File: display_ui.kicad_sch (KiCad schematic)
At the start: 68 parts, among them SW401 K2-1102SP-C4SC-04, SW402 K2-1102SP-C4SC-04, SW403 K2-1102SP-C4SC-04, SW404 K2-1102SP-C4SC-04, T401 AO3400A, T402 AO3400A, T403 AO3400A, T404 AO3400A, T405 AO3400A, X401 ER-TFT035-6

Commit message: changed pin types and fixed 3D-positions
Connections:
- removed net +3.3V: BUZZER401.1 (+), C409.2, C410.2, C411.2, D409.3 (A), D411.1 (K), R401.2, R404.3, R408.2, R411.3, R415.3, R416.2, R420.2, R428.1, R430.1, R433.1, R435.2, X401.13 (DOTCLK), X401.35 (RD), X401.40 (VDDI), X401.41 (VDDI), X401.42 (VCI)
- removed net GND: C401.1, C402.1, C403.1, C404.1, C405.1, C406.1, C407.1, C408.1, C409.1, C410.1, C411.1, D401.2 (C), D402.2 (C), D403.2 (C), D404.2 (C), D405.2 (C), D406.2 (C), D407.2 (C), D408.2 (C), D410.3 (VSS), R402.1, R404.1, R409.1, R411.1, R415.1, R417.1, R421.1, R429.2, R431.2, R434.2, T401.2 (S), T402.2 (S), T403.2 (S), T404.2 (S), T405.2 (S), X401.11 (VSYNC), X401.12 (HSYNC), X401.14 (DE), X401.15 (DB17), X401.16 (DB16), X401.17 (DB15), X401.18 (DB14), X401.19 (DB13), X401.20 (DB12), X401.21 (DB11), X401.22 (DB10), X401.23 (DB9), X401.24 (DB8), X401.25 (DB7), X401.26 (DB6), X401.27 (DB5), X401.28 (DB4), X401.29 (DB3), X401.30 (DB2), X401.31 (DB1), X401.32 (DB0), X401.43 (GND), X401.48 (GND), X401.49 (GND), X401.50 (GND)
- new net: C409.1, C410.1, C411.1
- new net: C409.2, C410.2, C411.2
- new net: R428.1, R430.1, R433.1
- new net: BUZZER401.1 (+), D411.1 (K)
- new net: X401.11 (VSYNC), X401.12 (HSYNC)
- new net: X401.14 (DE), X401.15 (DB17), X401.16 (DB16), X401.17 (DB15), X401.18 (DB14), X401.19 (DB13), X401.20 (DB12), X401.21 (DB11), X401.22 (DB10), X401.23 (DB9), X401.24 (DB8), X401.25 (DB7), X401.26 (DB6), X401.27 (DB5), X401.28 (DB4), X401.29 (DB3), X401.30 (DB2), X401.31 (DB1), X401.32 (DB0)
- new net: X401.40 (VDDI), X401.41 (VDDI), X401.42 (VCI)
- new net: X401.48 (GND), X401.49 (GND), X401.50 (GND)
- new net: R429.2, R431.2, R434.2

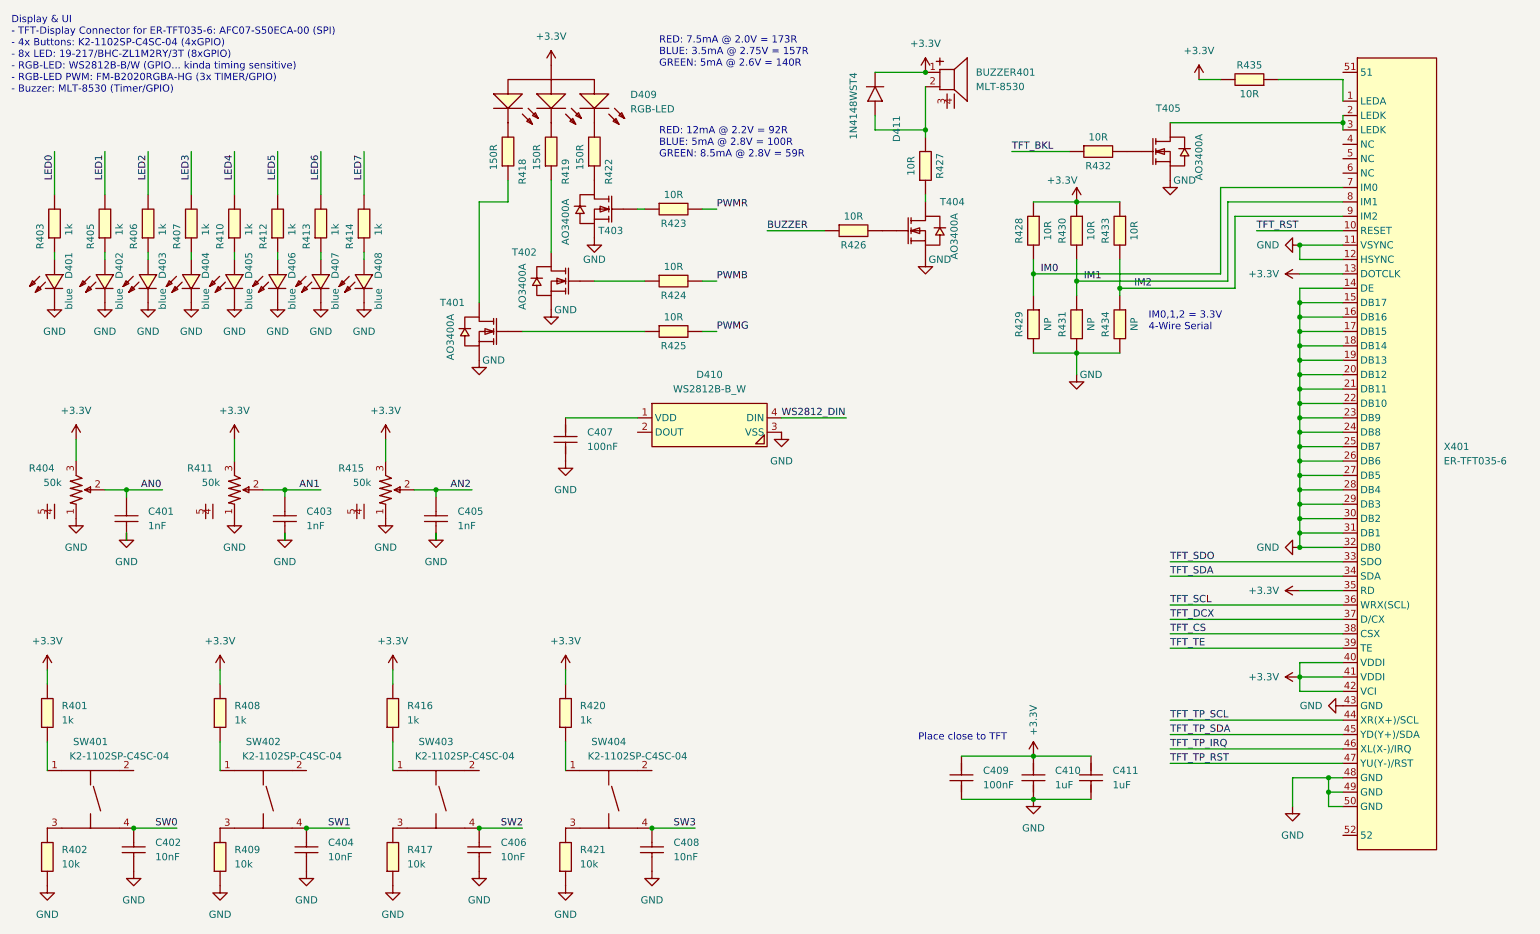
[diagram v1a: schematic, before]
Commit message: change all local labels to global labels.
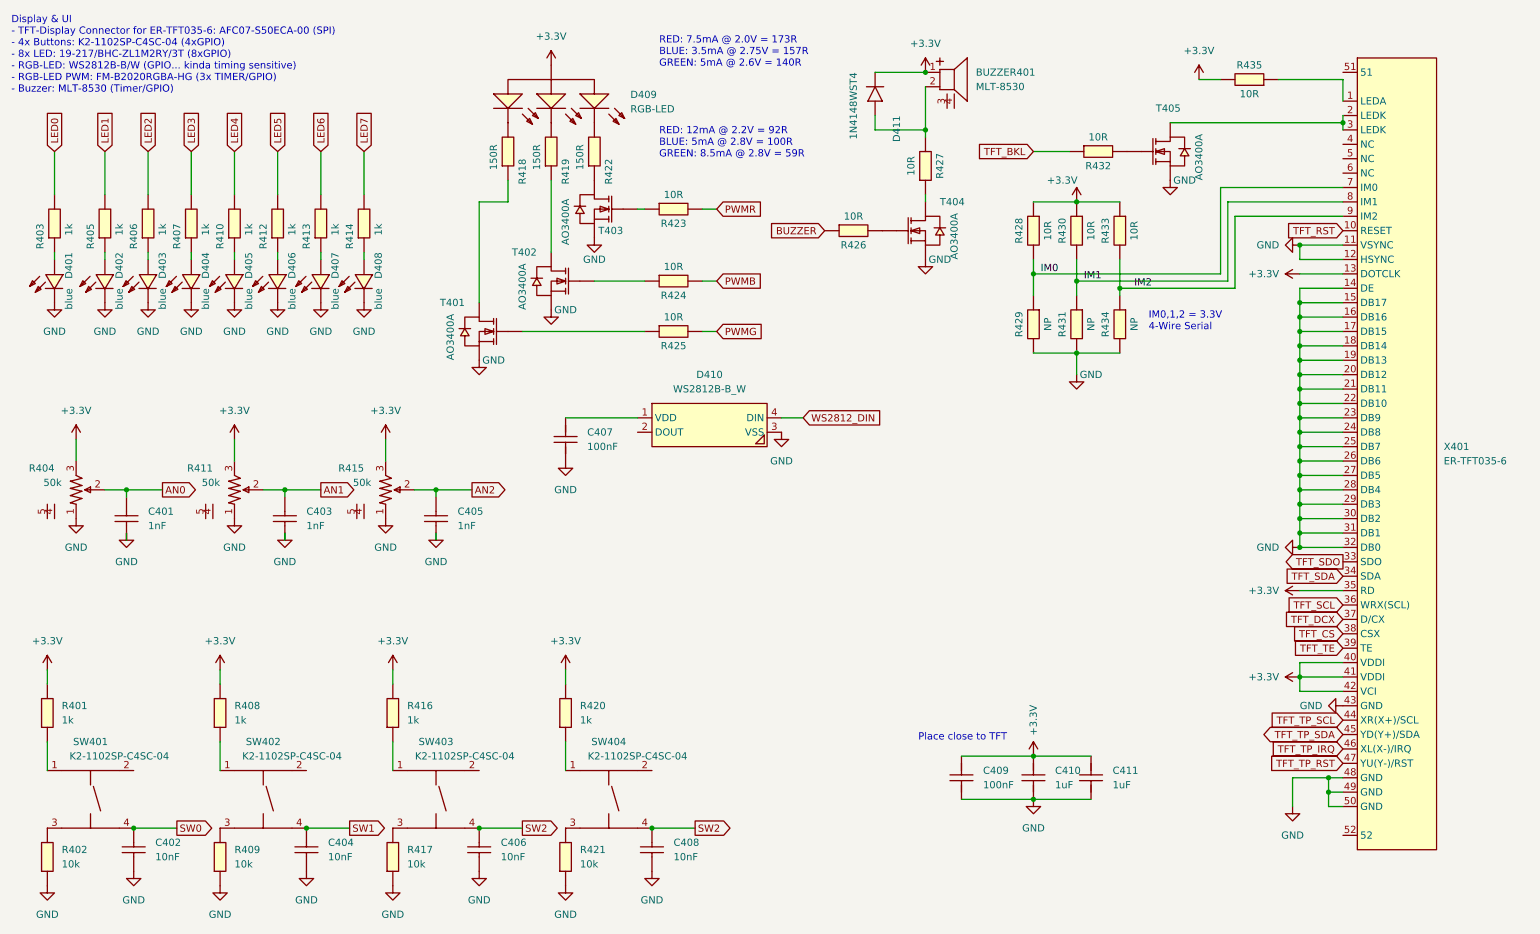
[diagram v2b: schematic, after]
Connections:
- net SW3 is gone; now on net SW2: C408.2, SW404.4

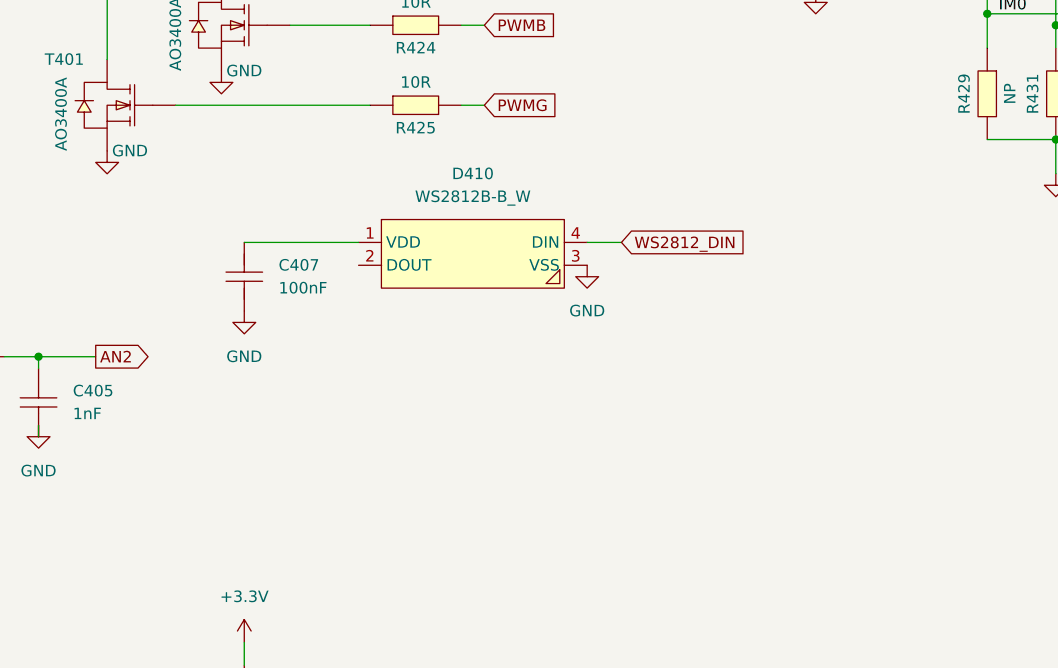
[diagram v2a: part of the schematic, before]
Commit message: add WS2812 Output Connector and add Level shifter to WS2812 input for 3.3V->5V conversion
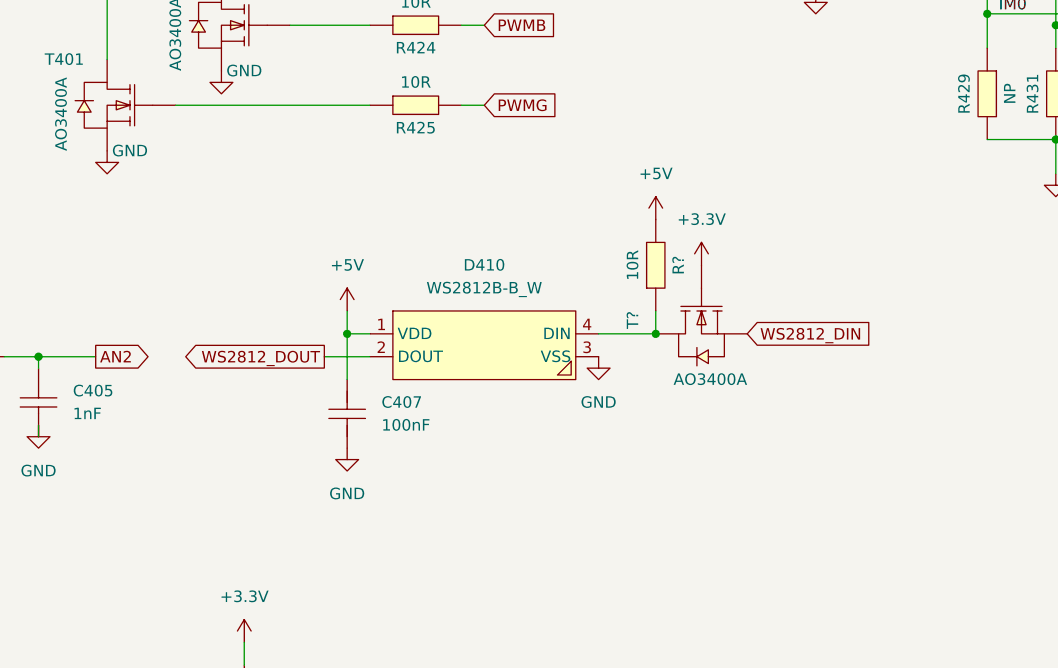
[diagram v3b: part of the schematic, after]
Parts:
- added R?: 10R, R0402, symbol eduboardv2:0402WGF100JTCE
- added T?: AO3400A, SOT-23-3_L2.9-W1.6-P1.90-LS2.8-BR, symbol eduboardv2:AO3400A
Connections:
- net WS2812_DIN: now also T?.2 (S); no longer D410.4 (DIN)
- net WS2812_DOUT: now reaches D410.2 (DOUT)
- new net: D410.4 (DIN), R?.1, T?.3 (D)
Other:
- moved on the sheet: C407, D410

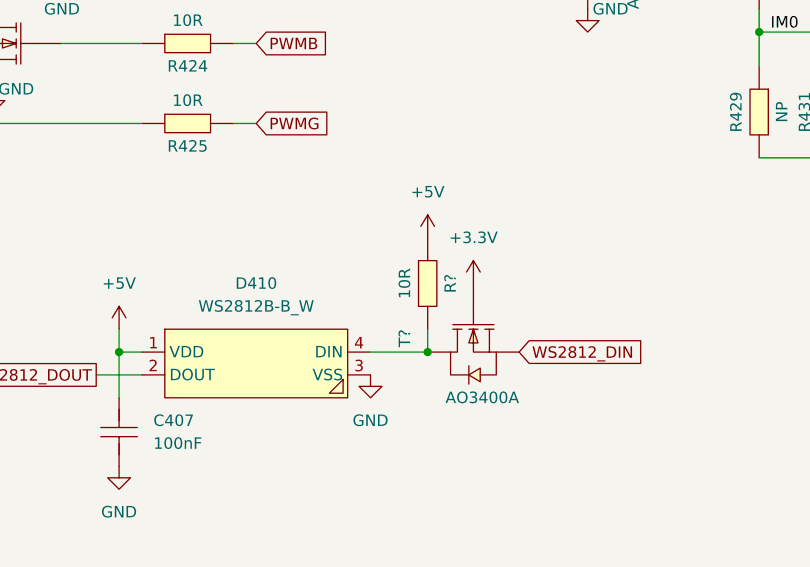
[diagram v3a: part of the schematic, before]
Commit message: fix Resistor Value for WS2812 level shifter
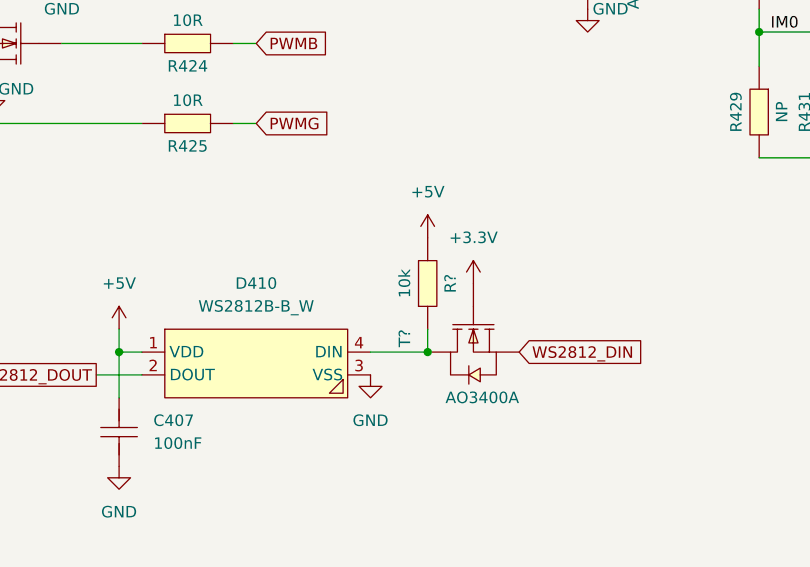
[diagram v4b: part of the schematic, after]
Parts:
- R?: value 10R -> 10k
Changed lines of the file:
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@@
     (in_bom yes) (on_board yes)
     (property "Reference" "R?" (id 0) (at 160.02 87.63 0))
-    (property "Value" "10R" (id 1) (at 154.94 87.63 0))
+    (property "Value" "10k" (id 1) (at 154.94 87.63 0))
     (property "Footprint" "R0402" (id 2) (at 165.1 87.63 0)
       (effects (font (size 1.27 1.27)) hide)

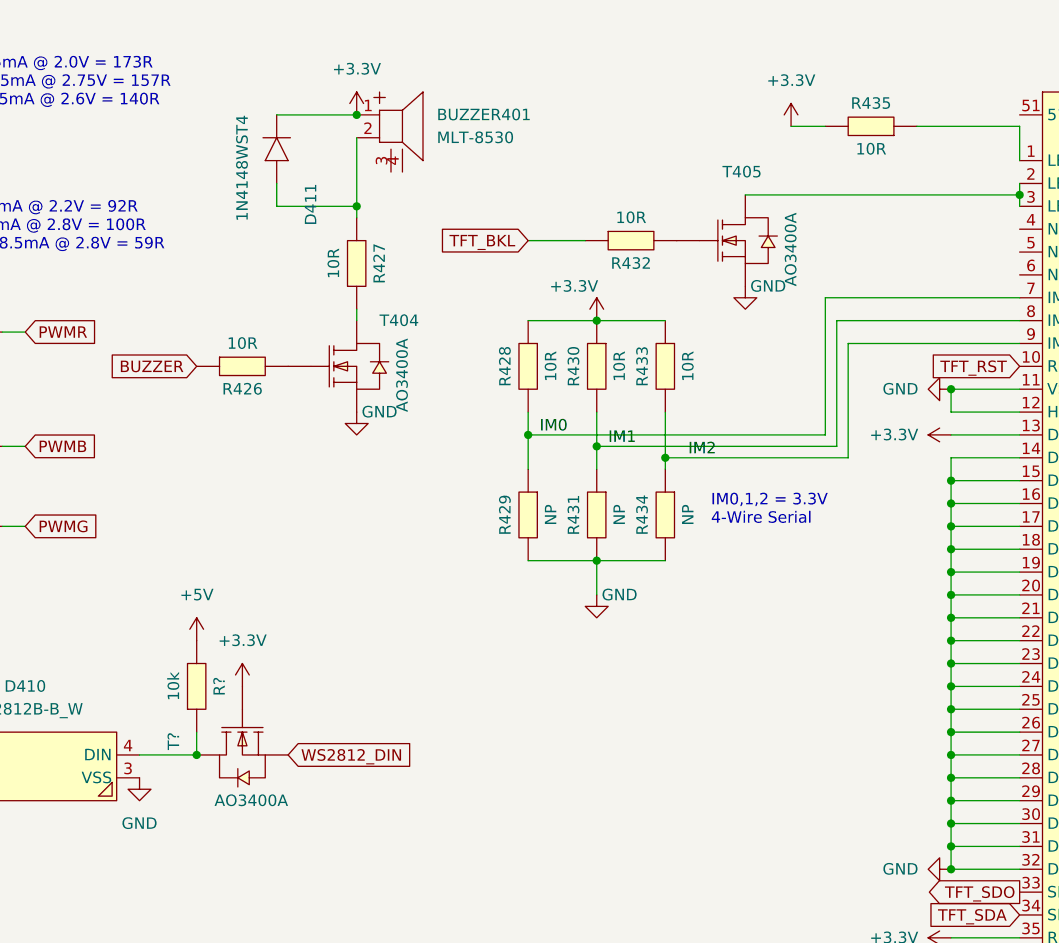
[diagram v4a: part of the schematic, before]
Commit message: reassign symbol references after page movements. Place in pcb
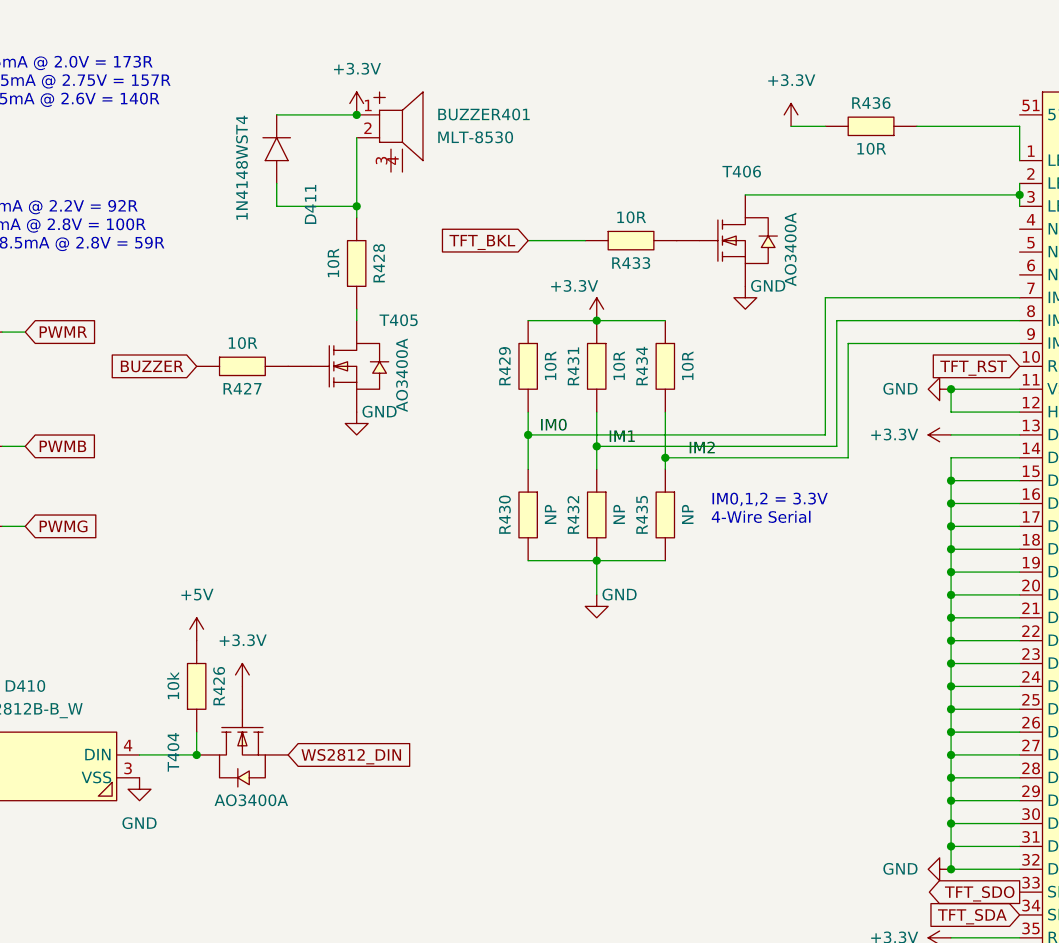
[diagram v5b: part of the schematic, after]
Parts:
- BUZZER401: footprint BUZ-SMD_4P-L8.5-W8.5-P8.50-TL -> eduboardv2:BUZ-SMD_4P-L8.5-W8.5-P8.50-TL
- C401, C402, C403, C404, C405, C406, C407, C408, C409, C410, C411: footprint C0402 -> eduboardv2:C0402
- D401, D402, D403, D404, D405, D406, D407, D408: footprint LED0603-R-RD_BLUE -> eduboardv2:LED0603-R-RD_BLUE
- D409: footprint LED-SMD_FM-B2020RGBA-HG -> eduboardv2:LED-SMD_FM-B2020RGBA-HG
- D410: footprint LED-SMD_4P-L5.0-W5.0-TL_WS2812B-B -> eduboardv2:LED-SMD_4P-L5.0-W5.0-TL_WS2812B-B
- D411: footprint SOD-323_L1.8-W1.3-LS2.5-RD -> eduboardv2:SOD-323_L1.8-W1.3-LS2.5-RD
- R401, R402, R403, R405, R406, R407, R408, R409, R410, R412, R413, R414, R416, R417, R418, R419, R420, R421, R422, R423, R424, R425: footprint R0402 -> eduboardv2:R0402
- R404, R411, R415: footprint RES-TH_RK09K1130AAU -> eduboardv2:RES-TH_RK09K1130AAU
- R426: renamed from R?; footprint R0402 -> eduboardv2:R0402
- R427: renamed from R426; footprint R0402 -> eduboardv2:R0402
- R428: renamed from R427; footprint R0402 -> eduboardv2:R0402
- R429: renamed from R428; footprint R0402 -> eduboardv2:R0402
- R430: renamed from R429; footprint R0402 -> eduboardv2:R0402
- R431: renamed from R430; footprint R0402 -> eduboardv2:R0402
- R432: renamed from R431; footprint R0402 -> eduboardv2:R0402
- R433: renamed from R432; footprint R0402 -> eduboardv2:R0402
- R434: renamed from R433; footprint R0402 -> eduboardv2:R0402
- R435: renamed from R434; footprint R0402 -> eduboardv2:R0402
- R436: renamed from R435; footprint R0402 -> eduboardv2:R0402
- SW401, SW402, SW403, SW404: footprint KEY-SMD_4P-L6.0-W6.0-P4.50-LS9.5-BL -> eduboardv2:KEY-SMD_4P-L6.0-W6.0-P4.50-LS9.5-BL
- T401, T402, T403: footprint SOT-23-3_L2.9-W1.6-P1.90-LS2.8-BR -> eduboardv2:SOT-23-3_L2.9-W1.6-P1.90-LS2.8-BR
- T404: renamed from T?; footprint SOT-23-3_L2.9-W1.6-P1.90-LS2.8-BR -> eduboardv2:SOT-23-3_L2.9-W1.6-P1.90-LS2.8-BR
- T405: renamed from T404; footprint SOT-23-3_L2.9-W1.6-P1.90-LS2.8-BR -> eduboardv2:SOT-23-3_L2.9-W1.6-P1.90-LS2.8-BR
- T406: renamed from T405; footprint SOT-23-3_L2.9-W1.6-P1.90-LS2.8-BR -> eduboardv2:SOT-23-3_L2.9-W1.6-P1.90-LS2.8-BR
- X401: footprint FPC-SMD_AFC07-S50ECA-00 -> eduboardv2:FPC-SMD_AFC07-S50ECA-00
